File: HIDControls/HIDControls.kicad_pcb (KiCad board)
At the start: 2 copper layers, 83.8 x 91.4 mm, 65 parts, among them J1 AnalogJoystick, M1 ModulePlug, M10 ModulePlug, M11 ModulePlug, M12 ModulePlug, M2 ModulePlug, M3 ModulePlug, M4 ModulePlug, M5 ModulePlug, M6 ModulePlug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

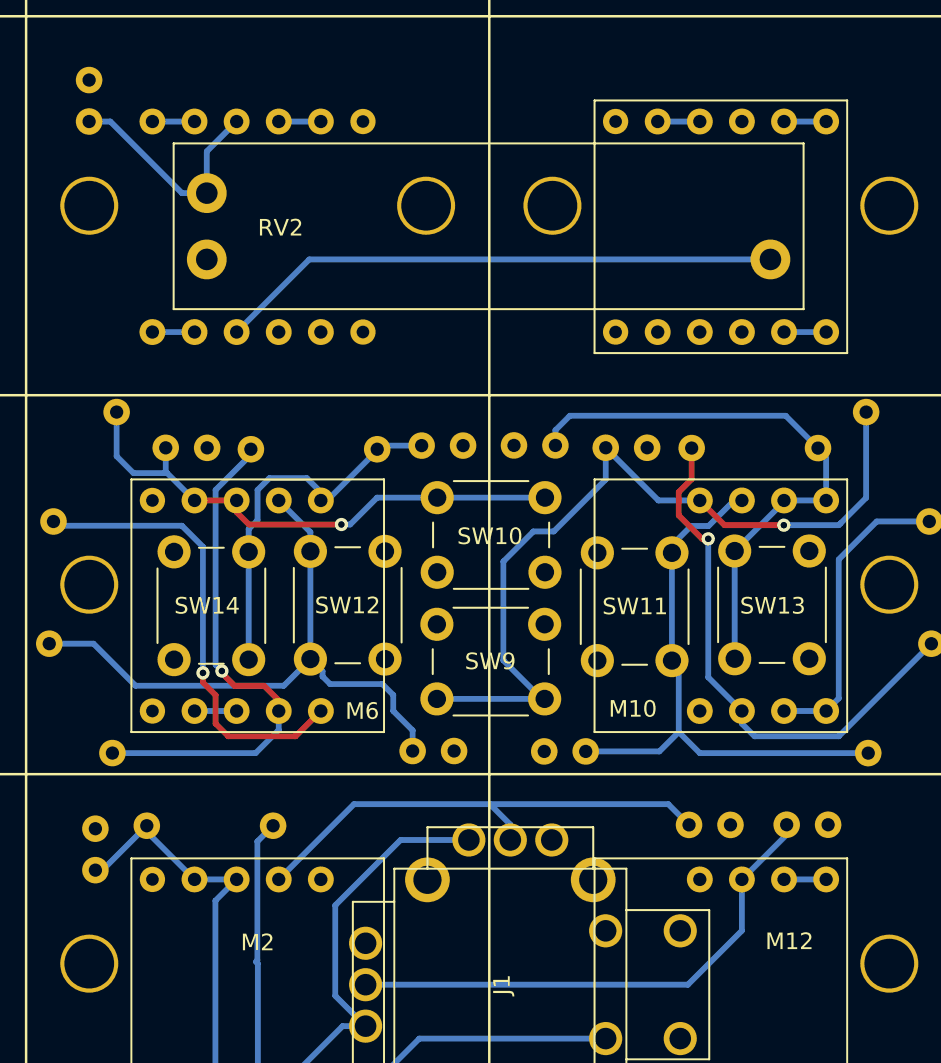
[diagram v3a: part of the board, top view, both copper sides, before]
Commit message: Added analog joystick device
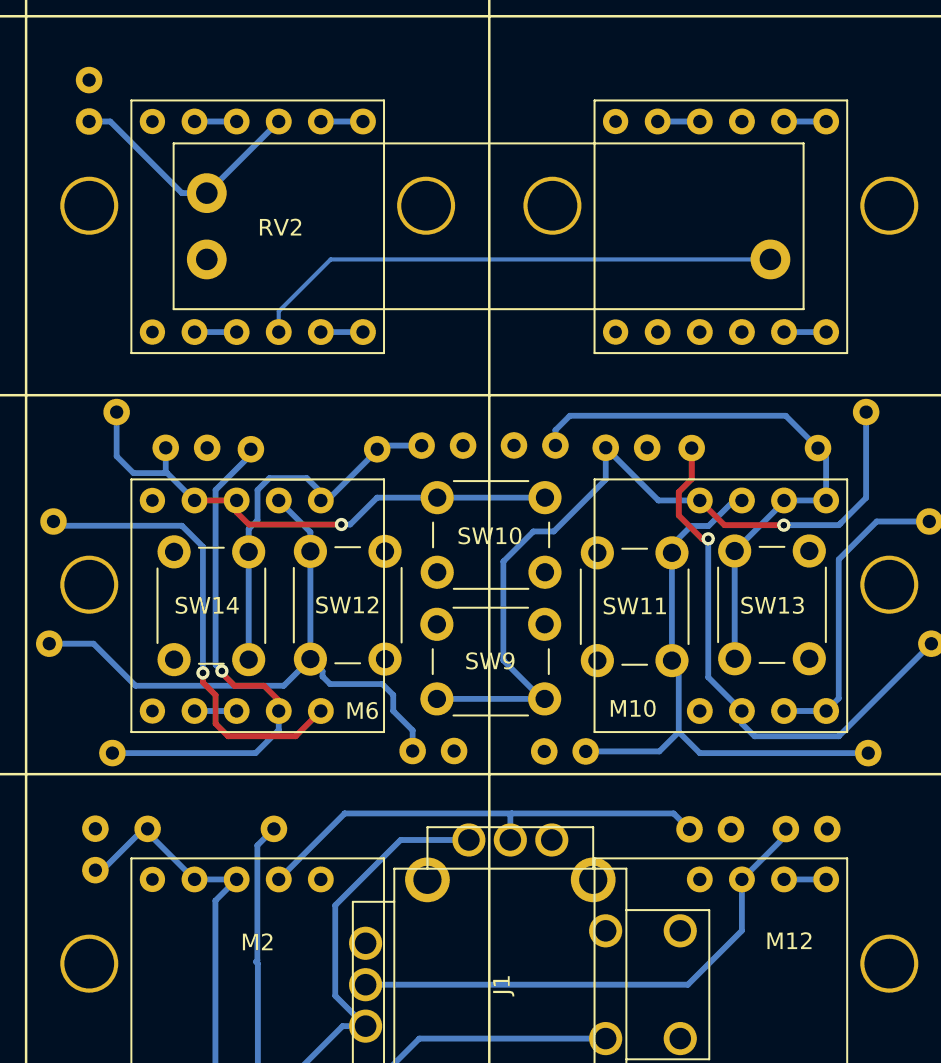
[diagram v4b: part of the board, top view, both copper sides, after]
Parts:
- M5: moved to F.Cu
- moved C3 0.27 mm to (156.9, 125.2)
- moved C10 0.26 mm to (165.2, 125.2)
- moved R3 0.20 mm to (131.8, 125.2)
- turned M5 to 0 degrees
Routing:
- net GND: track 2.54 -> 5.08 mm
- net Net-(M5-Pad2): track 34.0 -> 32.2 mm
- net Net-(J1-Pad2): track 29.8 -> 28.5 mm
- net Net-(C2-Pad2): track 14.0 -> 15.0 mm

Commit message: JLCPCB order 2023-22-02
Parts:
- moved C19 1.21 mm to (149.4, 120.4)
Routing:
- net Net-(C19-Pad1): track 34.8 -> 36.1 mm
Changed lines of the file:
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@@
   )
   (footprint "Capacitor_THT:C_Disc_D5.0mm_W2.5mm_P2.50mm" (layer "B.Cu")
-    (at 150.5966 120.5484 180)
+    (at 149.39 120.44 180)
     (descr "C, Disc series, Radial, pin pitch=2.50mm, , diameter*width=5*2.5mm^2, Capacitor, http://cdn-reichelt.de/documents/datenblatt/B300/DS_KERKO_TC.pdf")
     (tags "C Disc series Radial pin pitch 2.50mm  diameter 5mm width 2.5mm Capacitor")
@@
   (segment (start 156.21 119.38) (end 156.21 115.48) (width 0.35) (layer "B.Cu") (net 62))
   (segment (start 156.21 115.48) (end 155.8 115.07) (width 0.35) (layer "B.Cu") (net 62))
-  (segment (start 155.0416 120.5484) (end 156.21 119.38) (width 0.35) (layer "B.Cu") (net 62))
-  (segment (start 150.5966 120.5484) (end 155.0416 120.5484) (width 0.35) (layer "B.Cu") (net 62))
+  (segment (start 149.4984 120.5484) (end 155.0416 120.5484) (width 0.35) (layer "B.Cu") (net 62))
+  (segment (start 149.39 120.44) (end 149.4984 120.5484) (width 0.35) (layer "B.Cu") (net 62))
   (segment (start 155.8 108.57) (end 155.8 115.07) (width 0.35) (layer "B.Cu") (net 62))
   (segment (start 158.004 106.95) (end 156.956 106.95) (width 0.35) (layer "B.Cu") (net 62))
   (segment (start 155.8 108.106) (end 155.8 108.57) (width 0.35) (layer "B.Cu") (net 62))
+  (segment (start 155.0416 120.5484) (end 156.21 119.38) (width 0.35) (layer "B.Cu") (net 62))
   (segment (start 159.544 105.41) (end 158.004 106.95) (width 0.35) (layer "B.Cu") (net 62))
   (segment (start 132.08 105.41) (end 133.99 107.32) (width 0.35) (layer "B.Cu") (net 63))

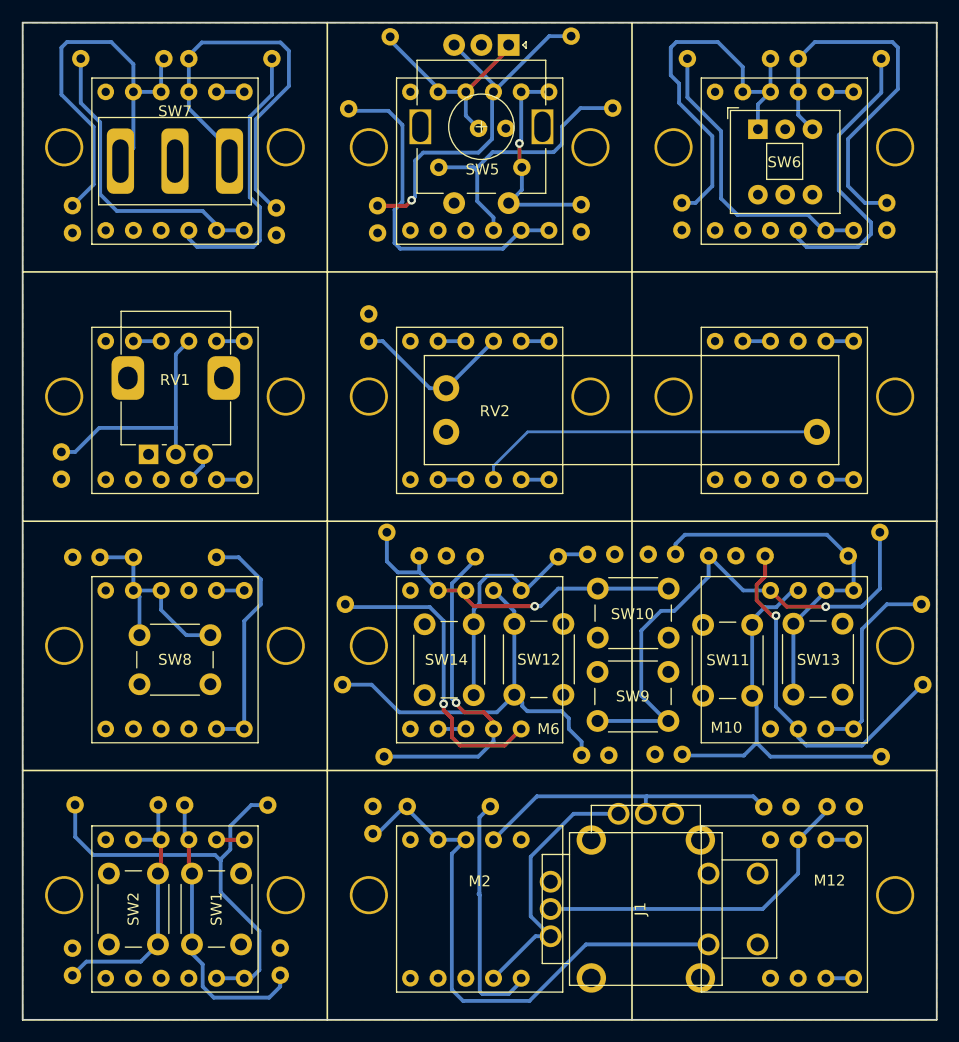
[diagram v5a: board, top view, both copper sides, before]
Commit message: Added CAD models
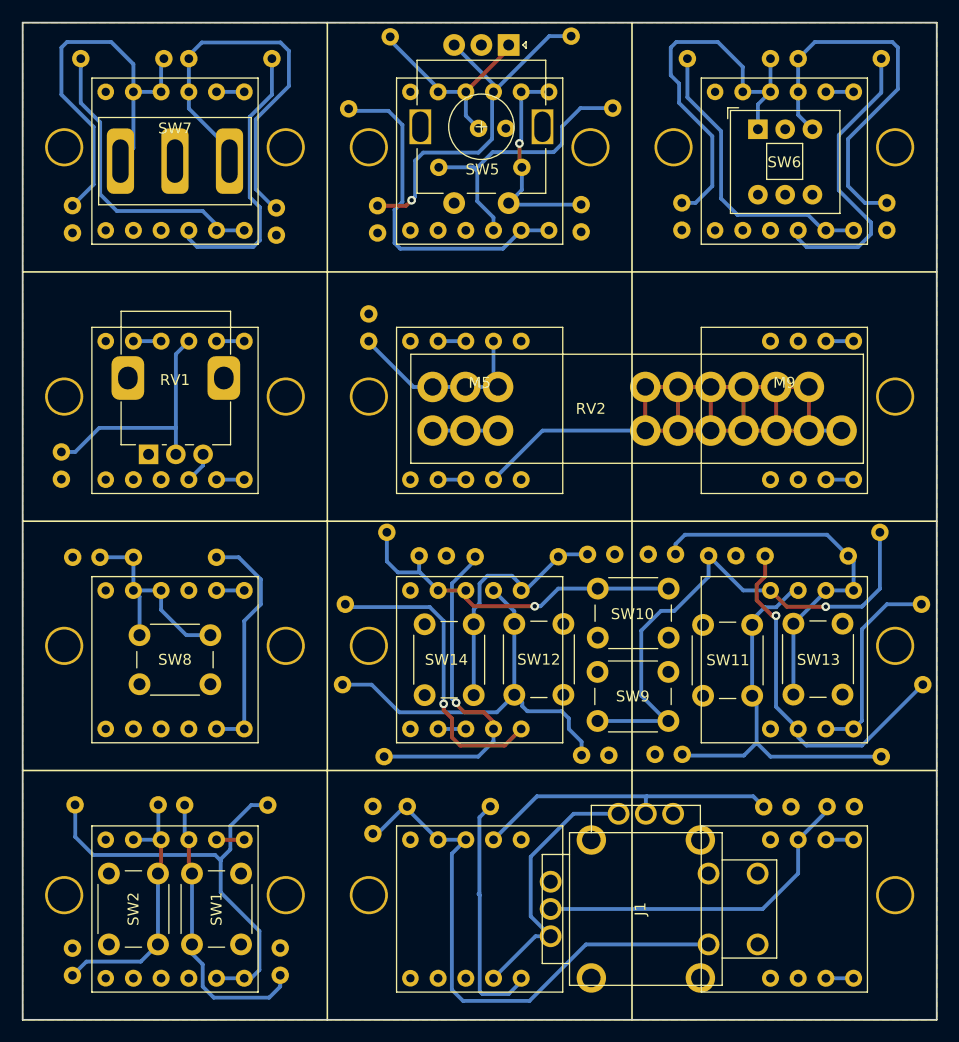
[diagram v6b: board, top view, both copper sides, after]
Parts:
- M5: footprint HIDControls:ModulePlug -> HIDControls:LeftPartModulePlug
- M9: footprint HIDControls:ModulePlug -> HIDControls:RightPartModulePlug
- RV2: footprint HIDPanel:Linear-Pot-2031N -> HIDControls:Linear-Pot-2031N
- SW7: footprint HIDPanel:5mmSPDTtoggle -> HIDControls:5mmSPDTtoggle
- moved RV2 1.25 mm to (126.5, 90.8)
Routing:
- net Net-(M5-Pad2): track 32.2 -> 73.8 mm
- net GND: track 5.08 -> 11.1 mm
- net Net-(C2-Pad2): track 15.0 -> 18.0 mm
- net unconnected-(M9-Pad4): track 2.54 -> 0.00 mm
- net unconnected-(M5-Pad6): track 2.54 -> 0.00 mm
- net unconnected-(M5-Pad3): track 2.54 -> 0.00 mm

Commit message: Working buttons, encoders
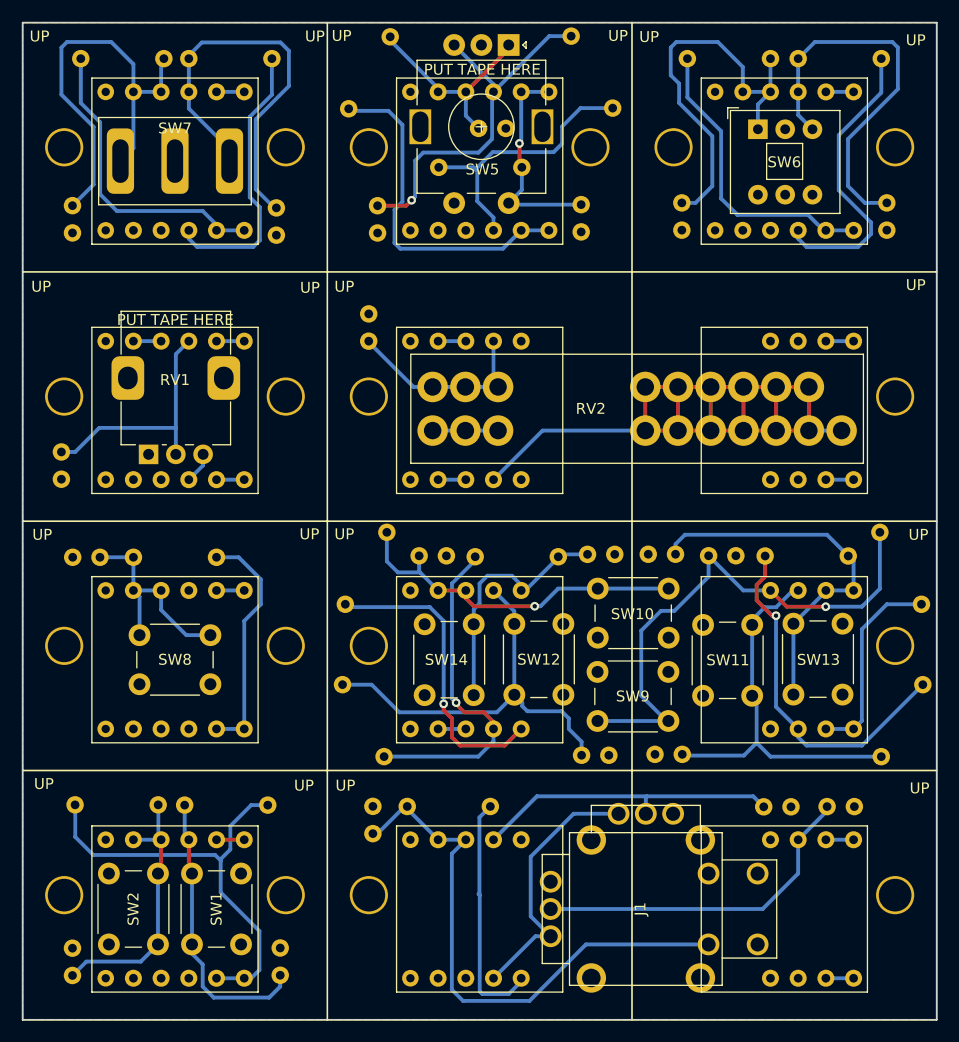
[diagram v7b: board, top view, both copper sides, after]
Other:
- board text added: "PUT TAPE HERE"
- board text added: "UP"
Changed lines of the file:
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@@
     (property "Sheetname" "")
     (attr exclude_from_pos_files)
-    (fp_text reference "M9" (at 0 -1.27 unlocked) (layer "F.SilkS")
+    (fp_text reference "M9" (at 0 -1.27 unlocked) (layer "F.SilkS") hide
       (effects (font (size 1 1) (thickness 0.15)))
     )
@@
     (property "Sheetname" "")
     (attr exclude_from_pos_files)
-    (fp_text reference "M5" (at 0 -1.27 unlocked) (layer "F.SilkS")
+    (fp_text reference "M5" (at 0 -1.27 unlocked) (layer "F.SilkS") hide
       (effects (font (size 1 1) (thickness 0.15)))
     )
@@
   (gr_line (start 88.9 144.78) (end 88.9 53.34) (layer "Edge.Cuts") (width 0.1))
   (gr_line (start 172.72 53.34) (end 172.72 144.78) (layer "Edge.Cuts") (width 0.1))
+  (gr_text "UP" (at 90.45 54.6) (layer "F.SilkS")
+    (effects (font (size 1 1) (thickness 0.15)))
+  )
+  (gr_text "UP" (at 90.6 77.55) (layer "F.SilkS")
+    (effects (font (size 1 1) (thickness 0.15)))
+  )
+  (gr_text "UP" (at 171.15 123.55) (layer "F.SilkS")
+    (effects (font (size 1 1) (thickness 0.15)))
+  )
+  (gr_text "UP" (at 114.7 123.3) (layer "F.SilkS")
+    (effects (font (size 1 1) (thickness 0.15)))
+  )
+  (gr_text "UP" (at 90.85 123.15) (layer "F.SilkS")
+    (effects (font (size 1 1) (thickness 0.15)))
+  )
+  (gr_text "UP" (at 118.15 54.55) (layer "F.SilkS")
+    (effects (font (size 1 1) (thickness 0.15)))
+  )
+  (gr_text "UP" (at 115.25 77.65) (layer "F.SilkS")
+    (effects (font (size 1 1) (thickness 0.15)))
+  )
+  (gr_text "UP" (at 170.8 54.95) (layer "F.SilkS")
+    (effects (font (size 1 1) (thickness 0.15)))
+  )
+  (gr_text "UP" (at 143.5 54.55) (layer "F.SilkS")
+    (effects (font (size 1 1) (thickness 0.15)))
+  )
+  (gr_text "UP" (at 90.7 100.3) (layer "F.SilkS")
+    (effects (font (size 1 1) (thickness 0.15)))
+  )
+  (gr_text "PUT TAPE HERE" (at 102.9 80.6) (layer "F.SilkS")
+    (effects (font (size 1 1) (thickness 0.15)))
+  )
+  (gr_text "UP" (at 115.2 100.25) (layer "F.SilkS")
+    (effects (font (size 1 1) (thickness 0.15)))
+  )
+  (gr_text "UP" (at 146.35 54.65) (layer "F.SilkS")
+    (effects (font (size 1 1) (thickness 0.15)))
+  )
+  (gr_text "UP" (at 171.05 100.3) (layer "F.SilkS")
+    (effects (font (size 1 1) (thickness 0.15)))
+  )
+  (gr_text "UP" (at 118.5 123.3) (layer "F.SilkS")
+    (effects (font (size 1 1) (thickness 0.15)))
+  )
+  (gr_text "UP" (at 118.4 100.25) (layer "F.SilkS")
+    (effects (font (size 1 1) (thickness 0.15)))
+  )
+  (gr_text "UP" (at 170.8 77.4) (layer "F.SilkS")
+    (effects (font (size 1 1) (thickness 0.15)))
+  )
+  (gr_text "UP" (at 115.7 54.6) (layer "F.SilkS")
+    (effects (font (size 1 1) (thickness 0.15)))
+  )
+  (gr_text "UP" (at 118.4 77.55) (layer "F.SilkS")
+    (effects (font (size 1 1) (thickness 0.15)))
+  )
+  (gr_text "PUT TAPE HERE" (at 131.05 57.65) (layer "F.SilkS")
+    (effects (font (size 1 1) (thickness 0.15)))
+  )
   (segment (start 109.22 95.25) (end 106.68 95.25) (width 0.35) (layer "B.Cu") (net 1))
   (segment (start 101.6 82.55) (end 99.06 82.55) (width 0.35) (layer "B.Cu") (net 2))

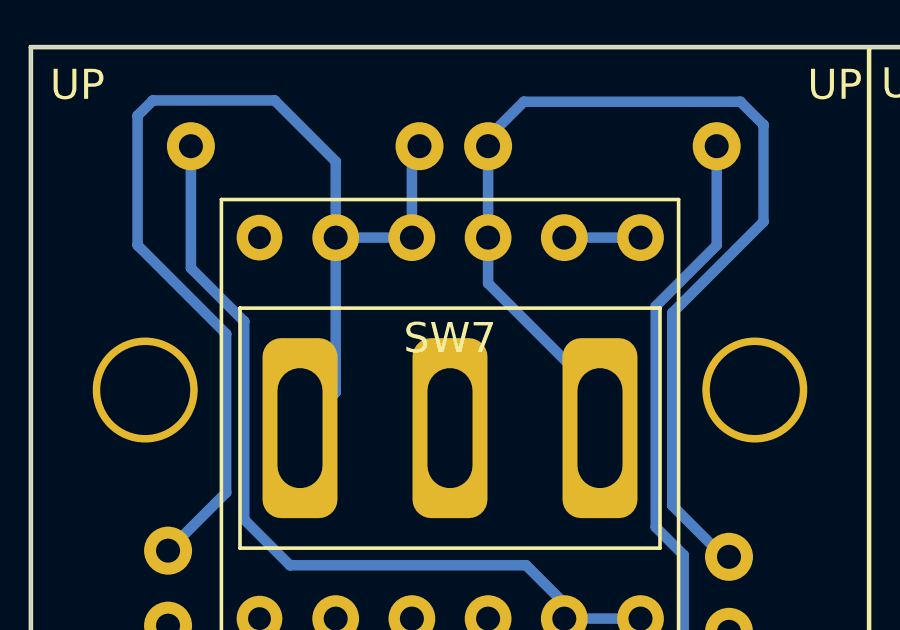
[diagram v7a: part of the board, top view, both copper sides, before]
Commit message: Modified HIDControls to include labels of parts
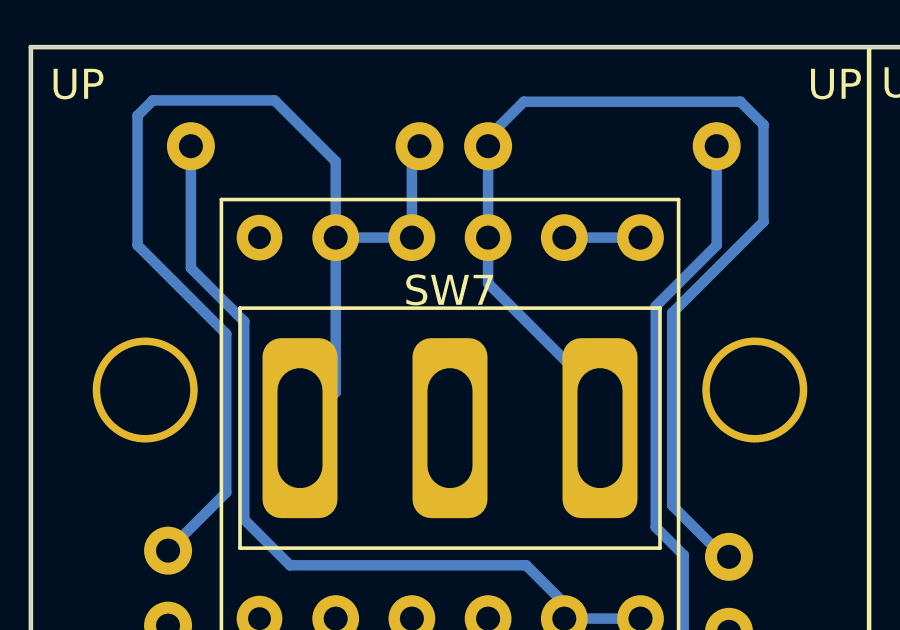
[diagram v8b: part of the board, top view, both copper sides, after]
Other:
- board text added: "2 X 6 MM BUTTON"
- board text added: "6 MM BUTTON"
- board text added: "6 MM BUTTONS"
- board text added: "ALPS RS301111A01G (OR SIMILAR 35 MM HOLE SPACING)"
- board text added: "DPAD"
- board text added: "EC12 ROTARY ENCODER"
- board text added: "PS4/XBOX ONE REPLACEMENT JOYSTICK"
- board text added: "RK09 POTENTIOMETER"
- board text added: "SPDT SWITCH/SS12D10"
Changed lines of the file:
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@@
     (property "Sheetname" "")
     (attr smd)
-    (fp_text reference "SW7" (at 0 -3 unlocked) (layer "F.SilkS")
+    (fp_text reference "SW7" (at 0 -4.572 unlocked) (layer "F.SilkS")
       (effects (font (size 1 1) (thickness 0.15)))
     )
@@
     (property "Sheetname" "")
     (attr through_hole)
-    (fp_text reference "C19" (at 4.5966 -0.0116 90) (layer "B.SilkS")
+    (fp_text reference "C19" (at -2.502 0 90) (layer "B.SilkS")
       (effects (font (size 1 1) (thickness 0.15)) (justify mirror))
     )
@@
   (gr_line (start 88.9 144.78) (end 88.9 53.34) (layer "Edge.Cuts") (width 0.1))
   (gr_line (start 172.72 53.34) (end 172.72 144.78) (layer "Edge.Cuts") (width 0.1))
+  (gr_text "2 X 6 MM BUTTON" (at 102.87 143.51) (layer "B.SilkS")
+    (effects (font (size 1 1) (thickness 0.15)) (justify mirror))
+  )
+  (gr_text "ALPS RS301111A01G (OR SIMILAR 35 MM HOLE SPACING)" (at 144.78 97.79) (layer "B.SilkS")
+    (effects (font (size 1 1) (thickness 0.15)) (justify mirror))
+  )
+  (gr_text "SPDT SWITCH/SS12D10" (at 158.75 74.93) (layer "B.SilkS")
+    (effects (font (size 1 1) (thickness 0.15)) (justify mirror))
+  )
+  (gr_text "SPDT SWITCH/SS12D10" (at 102.87 74.93) (layer "B.SilkS")
+    (effects (font (size 1 1) (thickness 0.15)) (justify mirror))
+  )
+  (gr_text "RK09 POTENTIOMETER" (at 102.87 97.79) (layer "B.SilkS")
+    (effects (font (size 1 1) (thickness 0.15)) (justify mirror))
+  )
+  (gr_text "DPAD" (at 158.75 120.65) (layer "B.SilkS")
+    (effects (font (size 1 1) (thickness 0.15)) (justify mirror))
+  )
+  (gr_text "6 MM BUTTON" (at 102.87 120.65) (layer "B.SilkS")
+    (effects (font (size 1 1) (thickness 0.15)) (justify mirror))
+  )
+  (gr_text "PS4/XBOX ONE REPLACEMENT JOYSTICK" (at 147.32 143.51) (layer "B.SilkS")
+    (effects (font (size 1 1) (thickness 0.15)) (justify mirror))
+  )
+  (gr_text "EC12 ROTARY ENCODER" (at 130.81 74.93) (layer "B.SilkS")
+    (effects (font (size 1 1) (thickness 0.15)) (justify mirror))
+  )
+  (gr_text "6 MM BUTTONS" (at 130.81 120.65) (layer "B.SilkS")
+    (effects (font (size 1 1) (thickness 0.15)) (justify mirror))
+  )
   (gr_text "UP" (at 90.45 54.6) (layer "F.SilkS")
     (effects (font (size 1 1) (thickness 0.15)))
